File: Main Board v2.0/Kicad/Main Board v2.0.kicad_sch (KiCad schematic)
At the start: 0 parts

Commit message: update
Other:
- sheet Control Logic ports: added A, BUS_CTRL, CPU_CTRL, D, MA, MEM_CTRL, MMU_CTRL; removed none
- sheet Expansion Bus ports: added A, BUS_CTRL, CPU_CTRL, D, MA; removed none
- sheet MMU ports: added A, D, MA, MMU_CTRL; removed none
- sheet Memory ports: added D, MA, MEM_CTRL; removed none

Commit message: schematic done*
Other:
- sheet CPU ports: added A[0..15], D[0..7]; removed A, CPU_CTRL, D
- sheet Control Logic ports: added A[0..15], D[0..7], MA[13..25]; removed A, BUS_CTRL, CPU_CTRL, D, MA, MEM_CTRL, MMU_CTRL
- sheet Expansion Bus ports: added A[0..15], D[0..7], MA[13..25]; removed A, BUS_CTRL, CPU_CTRL, D, MA
- sheet MMU ports: added A[0..15], D[0..7], MA[13..25]; removed A, D, MA, MMU_CTRL
- sheet Memory ports: added A[0..15], D[0..7], MA[13..25]; removed D, MA, MEM_CTRL

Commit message: board update
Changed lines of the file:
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@@
 			)
 		)
-		(pin "A[0..15]" input
+		(pin "A[0..15]" tri_state
 			(at 204.47 90.17 180)
 			(effects
@@
 			)
 		)
-		(pin "A[0..15]" input
+		(pin "A[0..15]" tri_state
 			(at 144.78 81.28 180)
 			(effects
@@
 			)
 		)
-		(pin "A[0..15]" output
+		(pin "A[0..15]" tri_state
 			(at 88.9 82.55 180)
 			(effects
@@
 			)
 		)
-		(pin "A[0..15]" bidirectional
+		(pin "A[0..15]" tri_state
 			(at 213.36 142.24 180)
 			(effects
@@
 			)
 		)
-		(pin "A[0..15]" input
+		(pin "A[0..15]" tri_state
 			(at 144.78 140.97 180)
 			(effects

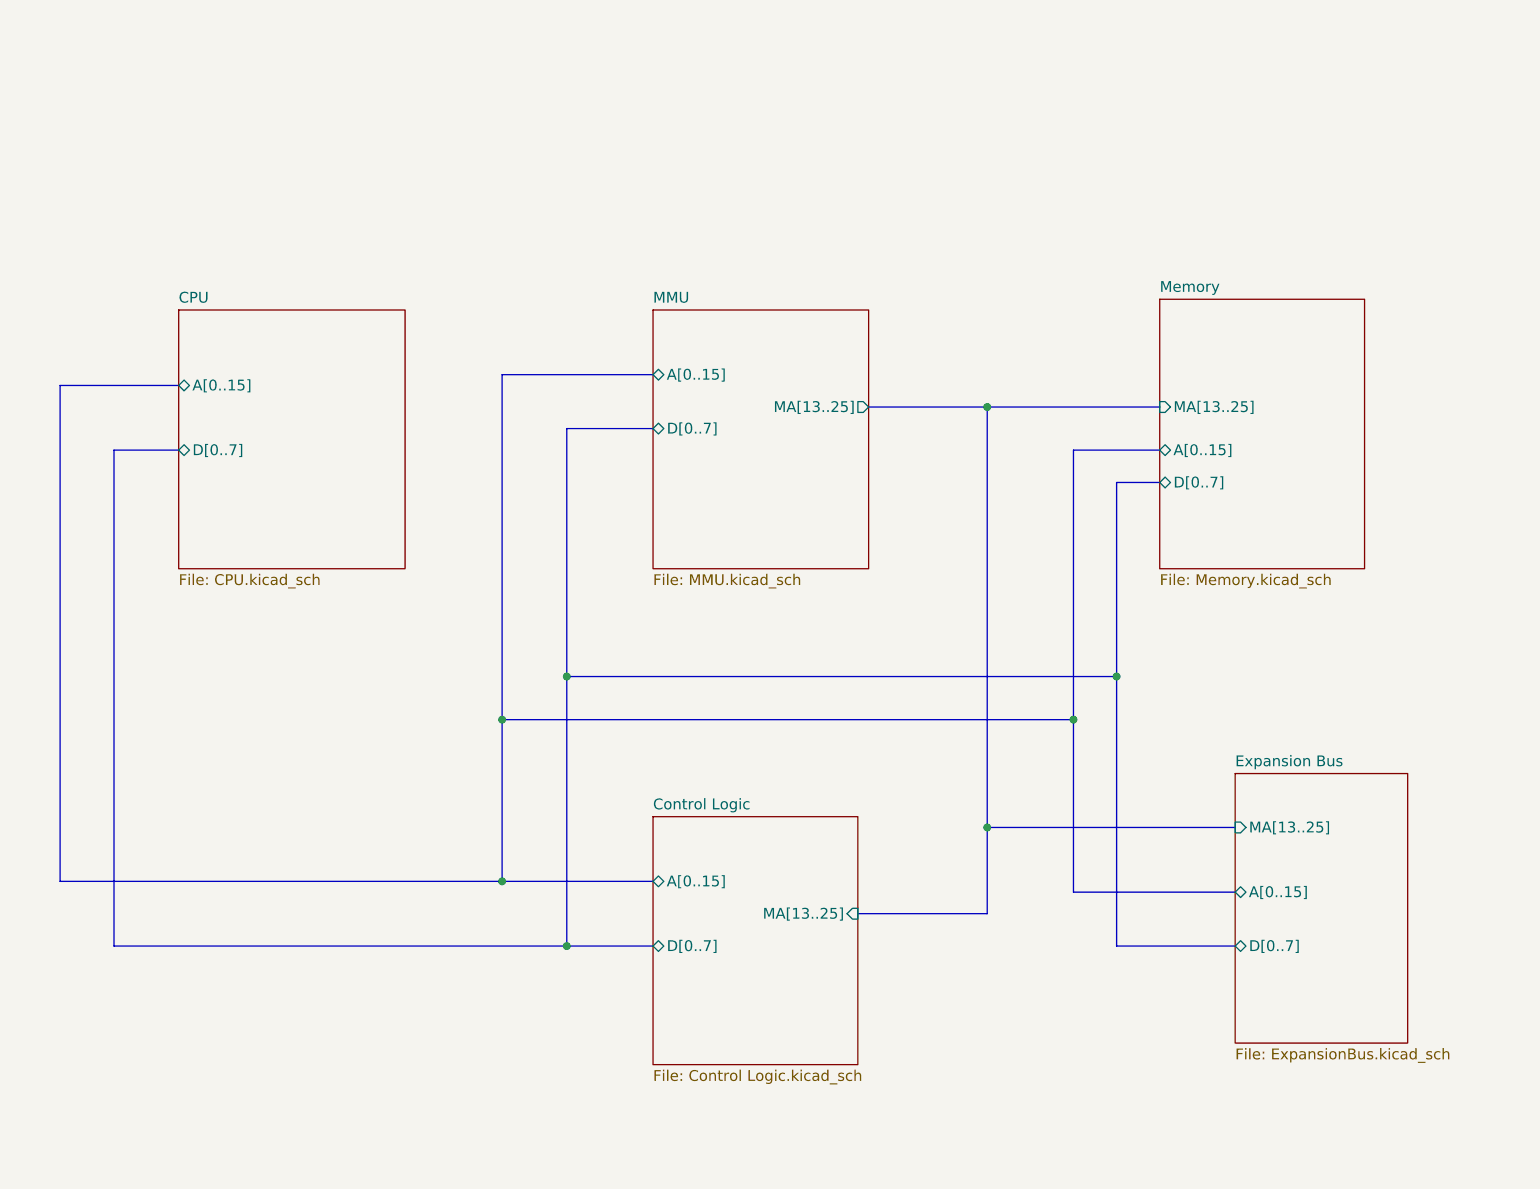
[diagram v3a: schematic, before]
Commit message: schematic update
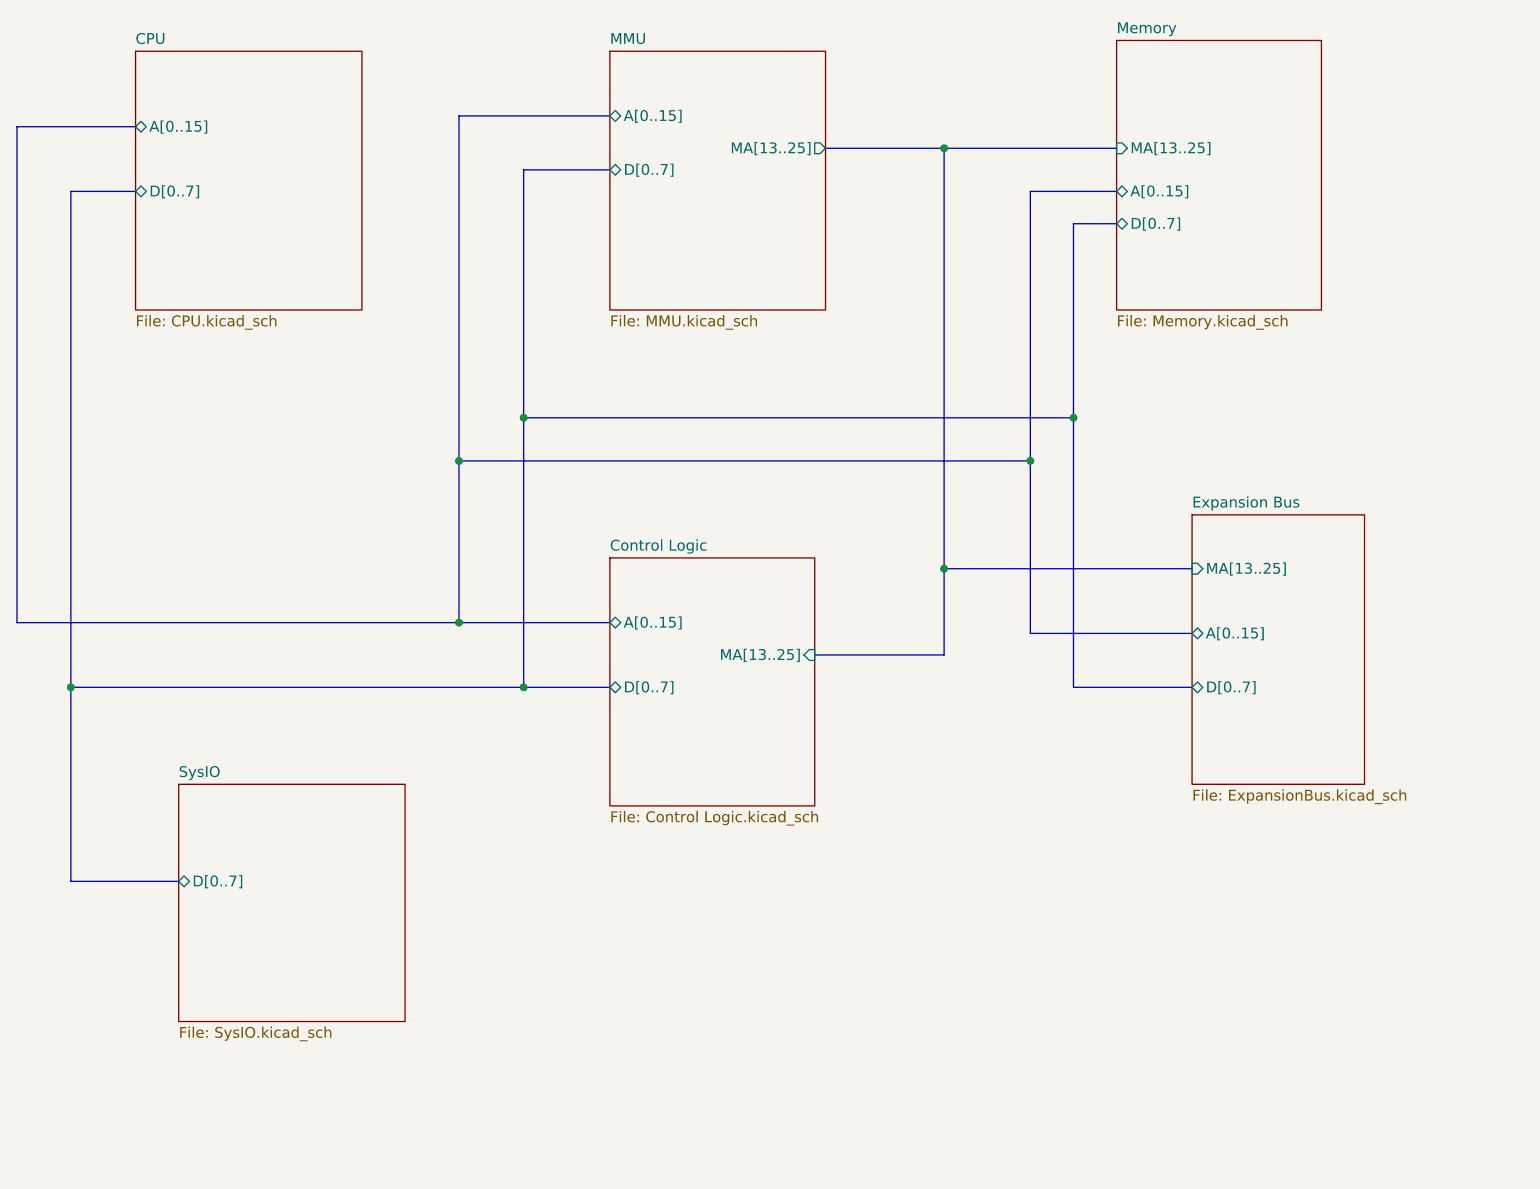
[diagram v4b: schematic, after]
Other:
- added sheet SysIO (SysIO.kicad_sch)

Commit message: board update
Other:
- sheet Control Logic ports: added MA[12..24]; removed MA[13..25]
- sheet Expansion Bus ports: added MA[12..24]; removed MA[13..25]
- sheet MMU ports: added MA[12..24]; removed MA[13..25]
- sheet Memory ports: added MA[12..24]; removed MA[13..25]
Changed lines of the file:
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@@
 			)
 		)
-		(pin "MA[13..25]" input
+		(pin "MA[12..24]" input
 			(at 199.39 54.61 180)
 			(effects
@@
 			)
 		)
-		(pin "MA[13..25]" output
+		(pin "MA[12..24]" output
 			(at 165.1 54.61 0)
 			(effects
@@
 			)
 		)
-		(pin "MA[13..25]" input
+		(pin "MA[12..24]" input
 			(at 208.28 104.14 180)
 			(effects
@@
 			)
 		)
-		(pin "MA[13..25]" input
+		(pin "MA[12..24]" input
 			(at 163.83 114.3 0)
 			(effects
